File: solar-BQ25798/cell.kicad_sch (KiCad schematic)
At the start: 12 parts, among them Q201 DMP2040UFDF-7, Q202 Q_PMOS_GSD, Q203 FS8205A_C908265, U201 BQ297xy

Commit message: BQ25798 WIP
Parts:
- removed Q201: DMP2040UFDF-7, Package_DFN_QFN:Diodes_UDFN2020-6_Type-F, symbol cacophony-library:DMP2040UFDF-7
- added Q201: DMP2035U-7, Package_TO_SOT_SMD:SOT-23, symbol cacophony-library:DMP2035U-7
- renumbered R203 to R202, R202 to R203, R207 to R204, R204 to R205, R205 to R206, R206 to R207
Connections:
- net CELL+: now also Q201.3 (D)
- net CELL_PROTECTED+: now also Q201.2 (S)
- net at Q202.3 (D), R202.2: now also Q201.1 (G)
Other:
- moved on the sheet: C201, Q202, Q203, R201, R202, R203, R204, R205, R206, R207, U201

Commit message: Solar battery WIP
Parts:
- renumbered R203 to R202, R202 to R203, R205 to R204, R206 to R205, R207 to R206, R204 to R207

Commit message: Tidy up of files
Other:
- note added: "Cell protection using the BQ29700"
- note added: "Protection against cell being inserted the wrong way."
- note added: "This resistor is to increase the voltage detected by the BQ29700 so the protection will trigger at a lower current."
- moved on the sheet: C201, Q201, Q202, Q203, R201, R202, R203, R204, R205, R206, R207, U201

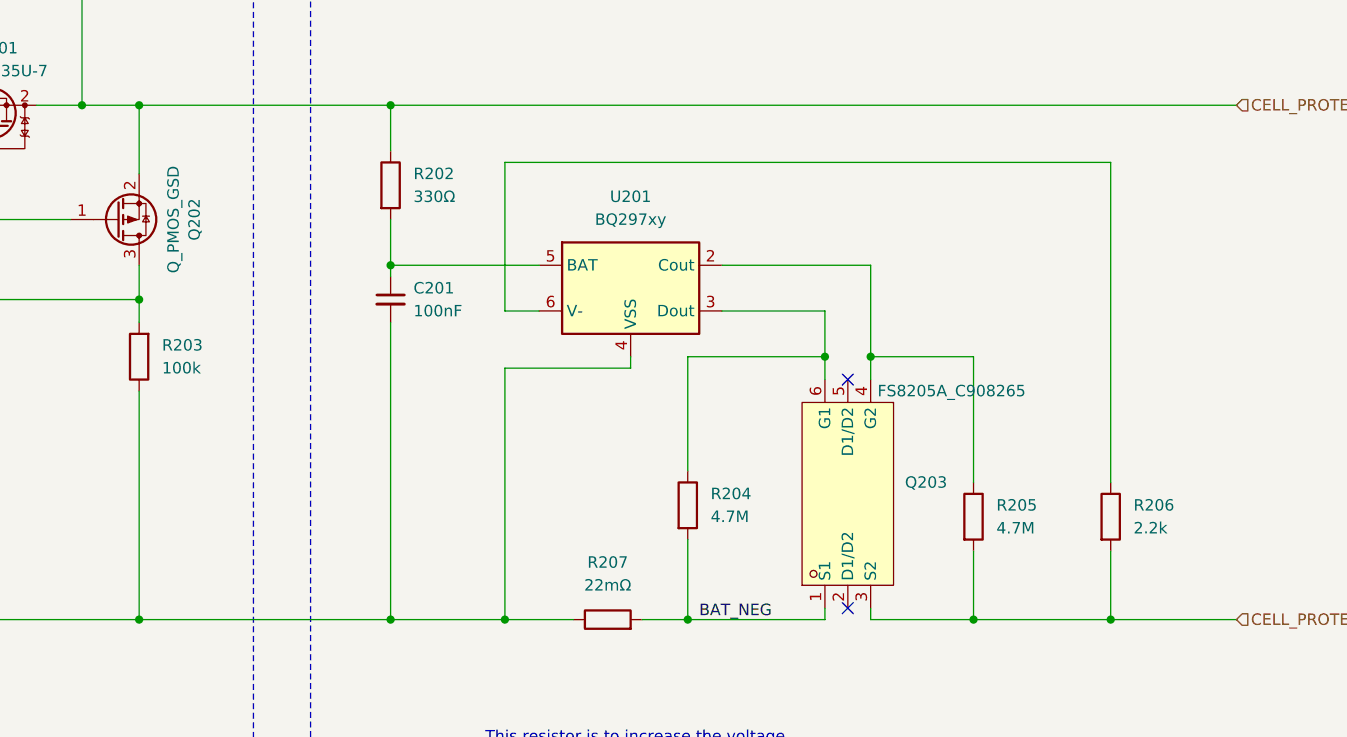
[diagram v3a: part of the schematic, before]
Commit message: Update battery PCB
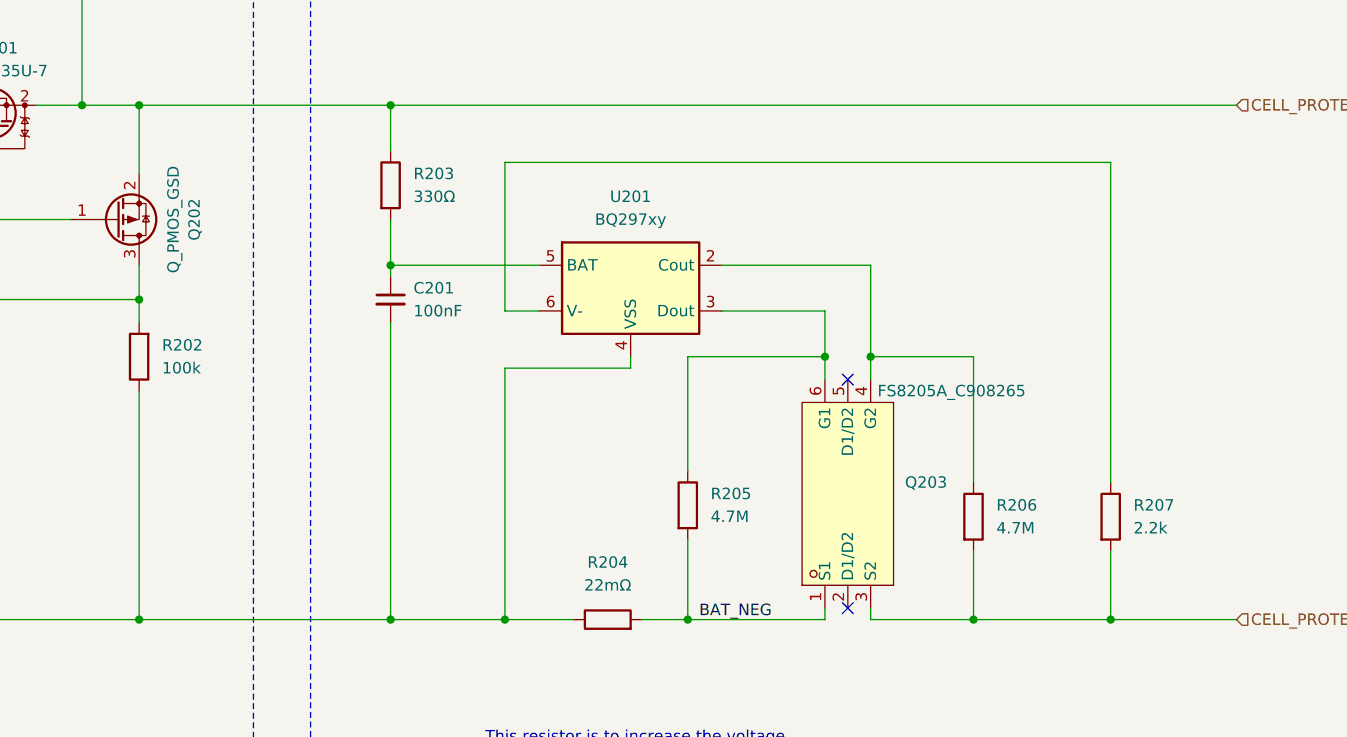
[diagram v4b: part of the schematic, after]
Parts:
- renumbered R203 to R202, R202 to R203, R207 to R204, R204 to R205, R205 to R206, R206 to R207

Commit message: Update 22mΩ component
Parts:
- R204: LCSC Part C247595 -> C2767461
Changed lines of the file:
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@@
 			)
 		)
-		(property "LCSC Part" "C247595"
+		(property "LCSC Part" "C2767461"
 			(at 172.72 132.08 0)
 			(effects

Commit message: Fix pin for serial out and other small fixes
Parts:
- C201: footprint Resistor_SMD:R_0402_1005Metric -> Capacitor_SMD:C_0402_1005Metric
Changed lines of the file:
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@@
 			)
 		)
-		(property "Footprint" "Resistor_SMD:R_0402_1005Metric"
+		(property "Footprint" "Capacitor_SMD:C_0402_1005Metric"
 			(at 148.59 96.52 0)
 			(hide yes)
